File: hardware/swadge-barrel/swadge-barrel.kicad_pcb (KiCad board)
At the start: 2 copper layers, 70.4 x 89.6 mm, 44 parts, among them J1 USB_B_Micro, SW1 SW_SPDT, U1 AP1117-33, U2 ESP-13-WROOM-02D, U3 BUS_PCIexpress, U4 OLED_CONNECTOR, U5 QMA6981, U6 OLED_DISPLAY

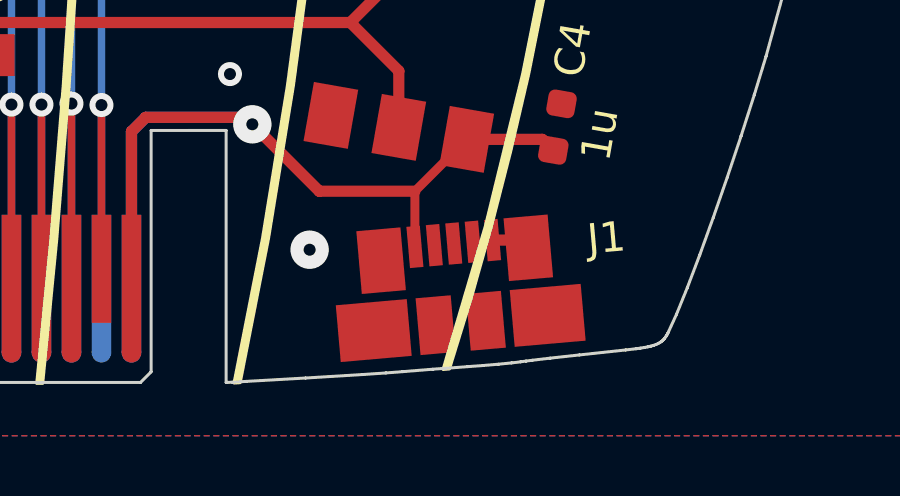
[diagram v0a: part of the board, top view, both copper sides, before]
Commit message: Added art to PCB
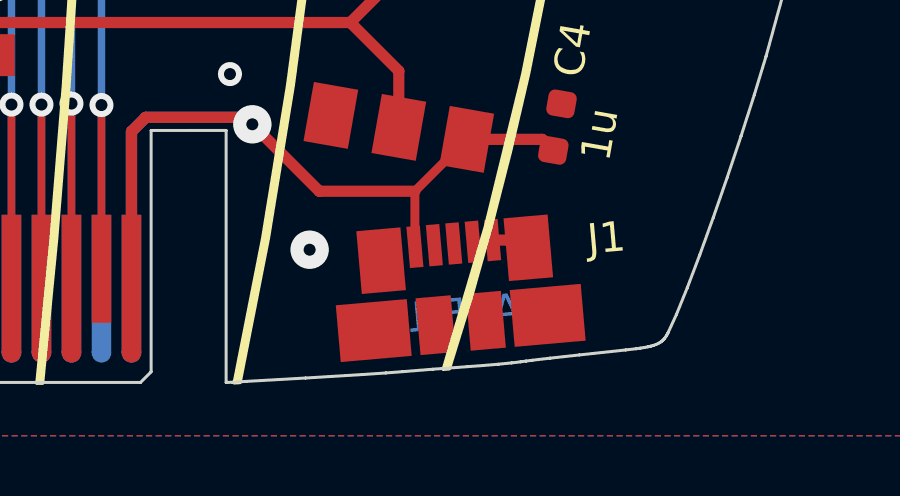
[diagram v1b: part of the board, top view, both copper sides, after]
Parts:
- added G***: LOGO, Swadge_Parts:mag-logo-fill, B.Cu at (171.1, 97.6)
- added G***: LOGO, Swadge_Parts:mag-logo-outline, B.Cu at (155.8, 64.8)
- added G***: LOGO, Swadge_Parts:funkus, B.Cu at (145.5, 98.2)
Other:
- board text added: "AEF'19"
- board text added: "Barrel 1.0.3"
- board text added: "First assembly, be gentle"
- board text removed: "Barrel 1.0.2"

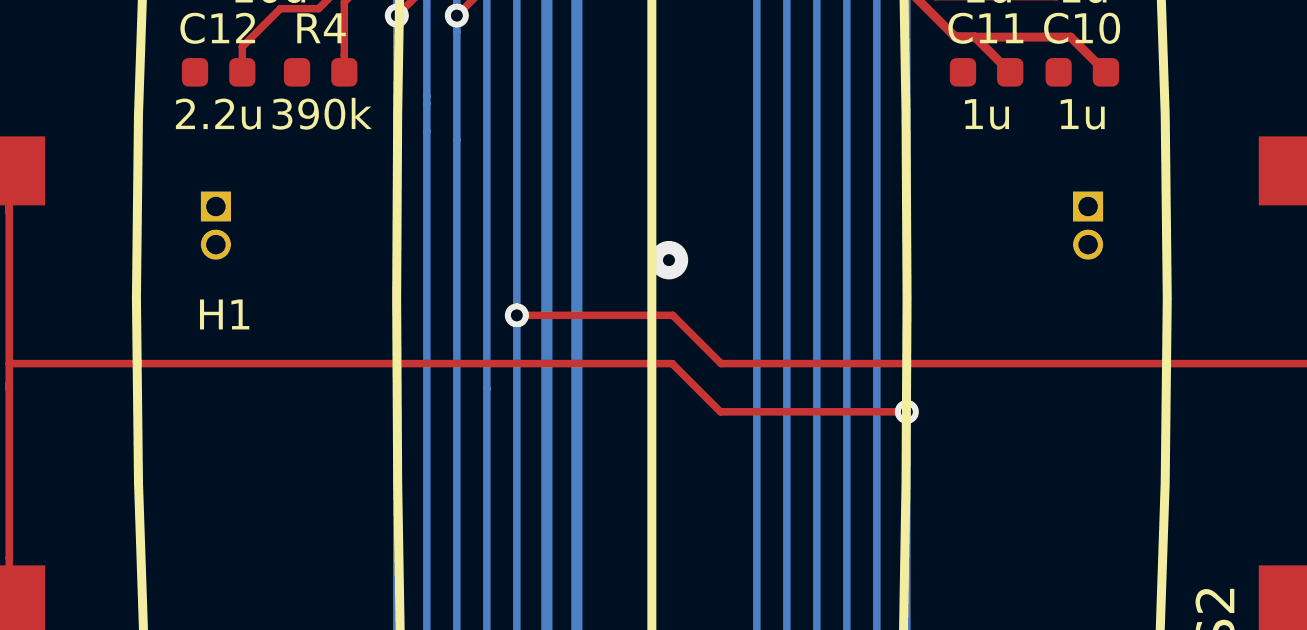
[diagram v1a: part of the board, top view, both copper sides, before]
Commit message: Added H2 part designator
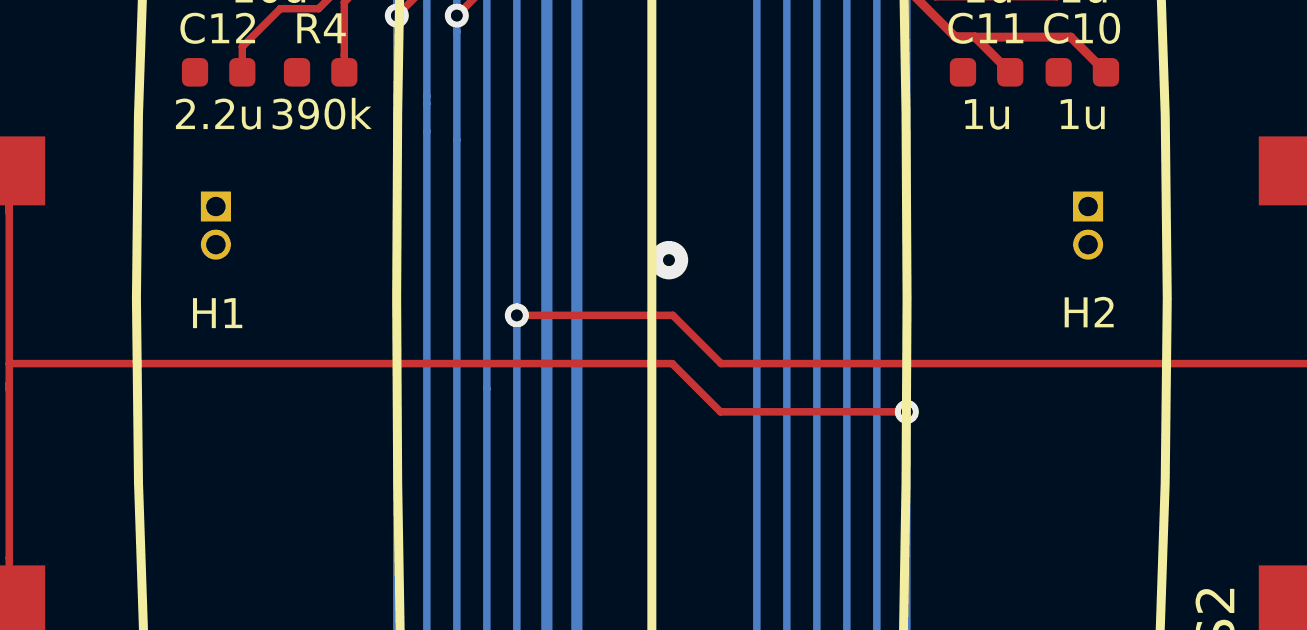
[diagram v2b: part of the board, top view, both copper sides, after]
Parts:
- added H2: Headband, Swadge_Parts:NULL, F.Cu at (99.5, 19.1)
- moved G*** 2.64 mm to (145.5, 100.9)
- moved G*** 1.60 mm to (154.2, 64.7)
- moved G*** 0.76 mm to (171.1, 98.4)

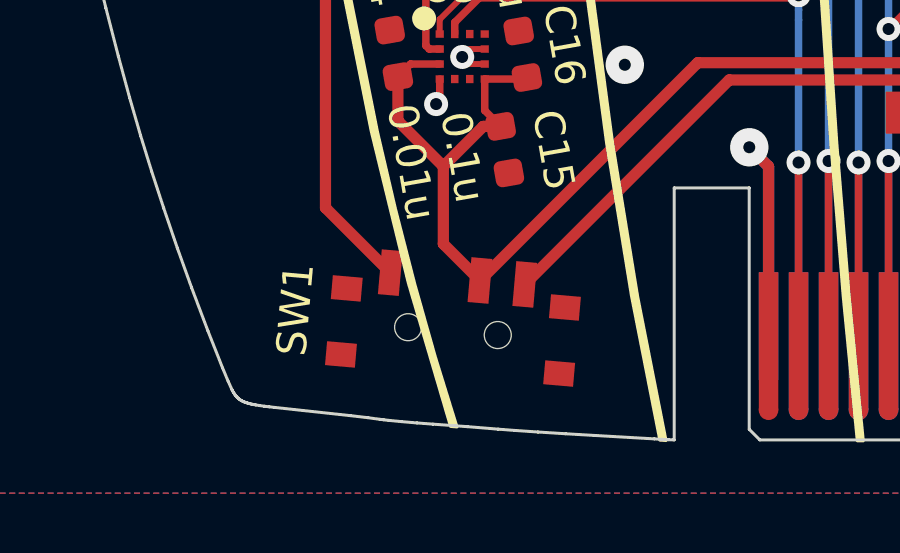
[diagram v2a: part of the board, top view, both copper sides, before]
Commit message: Added silk for power switch
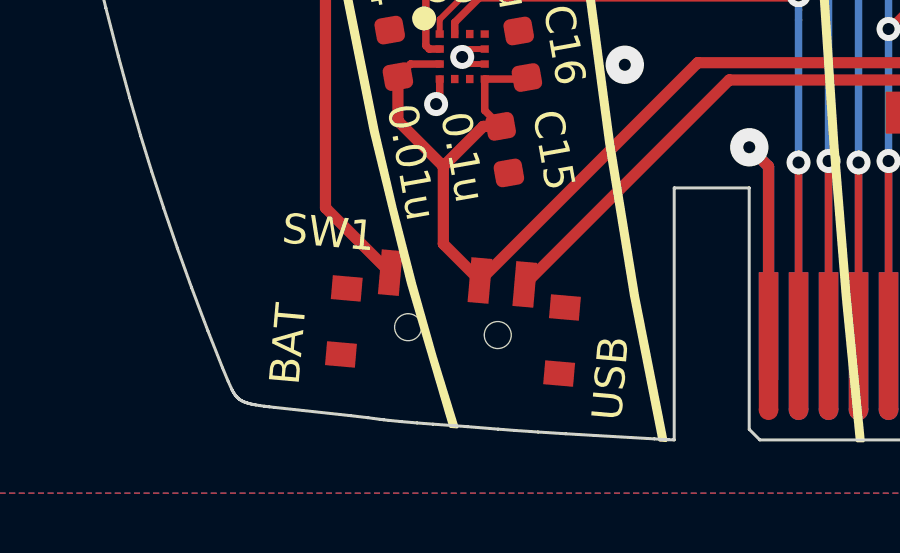
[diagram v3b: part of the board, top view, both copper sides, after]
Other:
- board text added: "BAT"
- board text added: "USB"
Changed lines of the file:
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@@
-(kicad_pcb (version 20171130) (host pcbnew "(5.1.2)-2")
+(kicad_pcb (version 20171130) (host pcbnew "(5.1.4)-1")
   (general
     (thickness 1.6)
-    (drawings 375)
+    (drawings 377)
     (tracks 481)
     (zones 0)
@@
   (page A4)
   (layers
-    (0 F.Cu signal hide)
+    (0 F.Cu signal)
     (31 B.Cu signal)
-    (32 B.Adhes user hide)
-    (33 F.Adhes user hide)
+    (32 B.Adhes user)
+    (33 F.Adhes user)
     (34 B.Paste user)
-    (35 F.Paste user hide)
+    (35 F.Paste user)
     (36 B.SilkS user)
     (37 F.SilkS user)
     (38 B.Mask user)
-    (39 F.Mask user hide)
-    (40 Dwgs.User user hide)
-    (41 Cmts.User user hide)
-    (42 Eco1.User user hide)
-    (43 Eco2.User user hide)
+    (39 F.Mask user)
+    (40 Dwgs.User user)
+    (41 Cmts.User user)
+    (42 Eco1.User user)
+    (43 Eco2.User user)
     (44 Edge.Cuts user)
-    (45 Margin user hide)
+    (45 Margin user)
     (46 B.CrtYd user)
-    (47 F.CrtYd user hide)
+    (47 F.CrtYd user)
     (48 B.Fab user)
-    (49 F.Fab user hide)
+    (49 F.Fab user)
   )
   (setup
@@
     (descr "Ultraminiature Surface Mount Slide Switch")
     (attr smd)
-    (fp_text reference SW1 (at -5.295814 0.070429 85) (layer F.SilkS)
+    (fp_text reference SW1 (at -4.416177 -2.581729 175) (layer F.SilkS)
       (effects (font (size 1 1) (thickness 0.15)))
     )
@@
     )
   )
+  (gr_text USB (at 130.72872 140.94968 85) (layer F.SilkS)
+    (effects (font (size 1 1) (thickness 0.15)))
+  )
+  (gr_text BAT (at 119.97944 139.80668 85) (layer F.SilkS)
+    (effects (font (size 1 1) (thickness 0.15)))
+  )
   (gr_text AEF'19 (at 165.608 140.7414 5) (layer B.Cu)

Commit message: Replaces test text with URL
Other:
- board text added: "http://swadge.com/super2020/"
- board text removed: "First assembly, be gentle"
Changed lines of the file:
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@@
   (layers
     (0 F.Cu signal)
-    (31 B.Cu signal)
+    (31 B.Cu signal hide)
     (32 B.Adhes user)
     (33 F.Adhes user)
@@
     (effects (font (size 1 1) (thickness 0.15)) (justify mirror))
   )
-  (gr_text "First assembly, be gentle" (at 145.5166 130.3528) (layer B.SilkS)
-    (effects (font (size 3 3) (thickness 0.3)) (justify mirror))
+  (gr_text http://swadge.com/super2020/ (at 145.5166 130.3528) (layer B.SilkS)
+    (effects (font (size 2.4 2.4) (thickness 0.3)) (justify mirror))
   )
   (gr_poly (pts (xy 151.835884 53.442005) (xy 152.304799 58.253345) (xy 152.716938 63.355966) (xy 153.070529 68.716613) (xy 153.363802 74.302033) (xy 153.594985 80.078971) (xy 153.762308 86.014172) (xy 153.864001 92.074382) (xy 153.898292 98.226347) (xy 153.863941 104.382621) (xy 153.762073 110.446949) (xy 153.594472 116.386018) (xy 153.362917 122.166516) (xy 153.069189 127.755129) (xy 152.715071 133.118544) (xy 152.302343 138.223448) (xy 151.832786 143.036528) (xy 152.033805 143.036528) (xy 152.503252 138.22122) (xy 152.915833 133.115002) (xy 153.269782 127.751049) (xy 153.563335 122.162535) (xy 153.794726 116.382634) (xy 153.962191 110.444519) (xy 154.063965 104.381366) (xy 154.098281 98.226347) (xy 154.064017 92.076122) (xy 153.962398 86.017523) (xy 153.795186 80.083666) (xy 153.564143 74.307669) (xy 153.271032 68.722646) (xy 152.917614 63.361715) (xy 152.505652 58.25799) (xy 152.036907 53.444589) (xy 151.835884 53.442005)) (layer F.SilkS) (width 0.099999))
